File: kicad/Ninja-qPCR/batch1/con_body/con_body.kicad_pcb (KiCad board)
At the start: 2 copper layers, 22 x 26 mm, 6 parts, among them J1 Conn_01x04_Male, U1 Conn_02x05

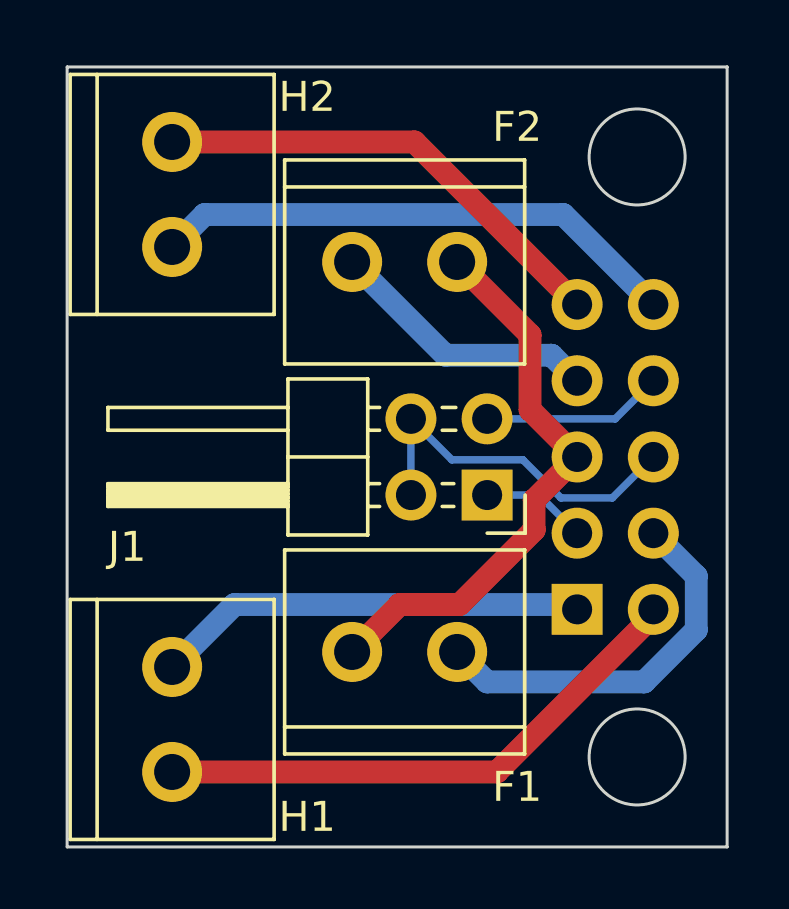
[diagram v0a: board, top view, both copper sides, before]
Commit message: add schematics of test boards
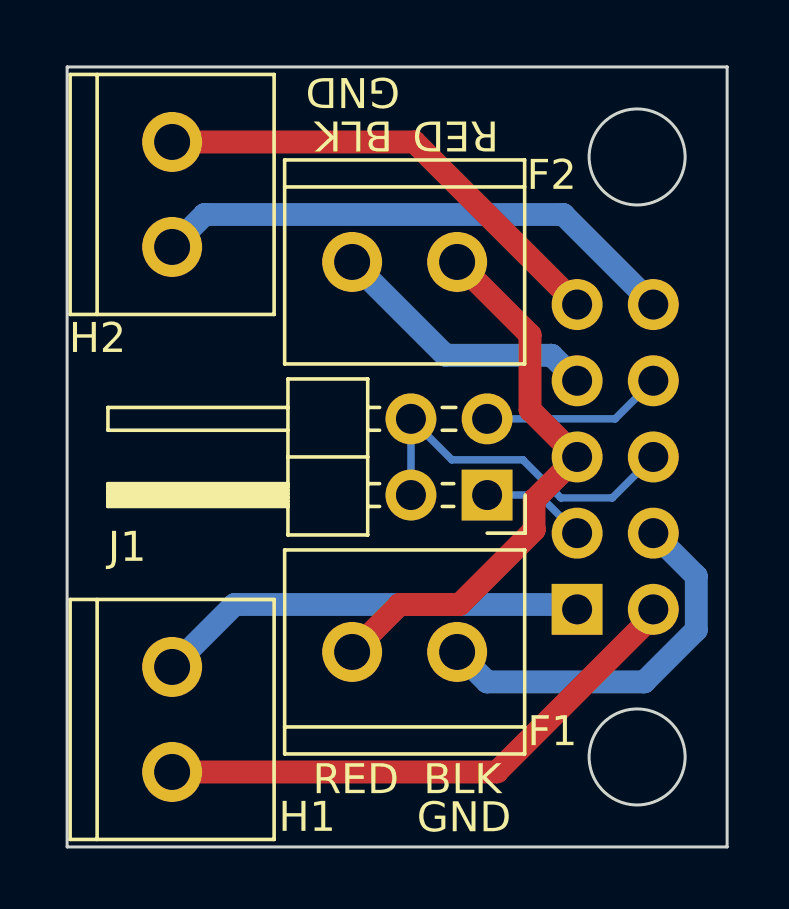
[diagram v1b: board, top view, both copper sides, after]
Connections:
- net FAN1 renamed FAN_BLACK_GND1
- net FAN2 renamed FAN_BLACK_GND2
- net FAN_VCC renamed FAN_RED_VCC
- net THERM1 renamed THERM_WELL
- net THERM2 renamed THERM_EXT3
- net THERM_GND renamed GND
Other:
- board text added: "BLK"
- board text added: "GND"
- board text added: "RED"
